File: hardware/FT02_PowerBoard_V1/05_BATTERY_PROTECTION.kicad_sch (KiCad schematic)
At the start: 0 parts

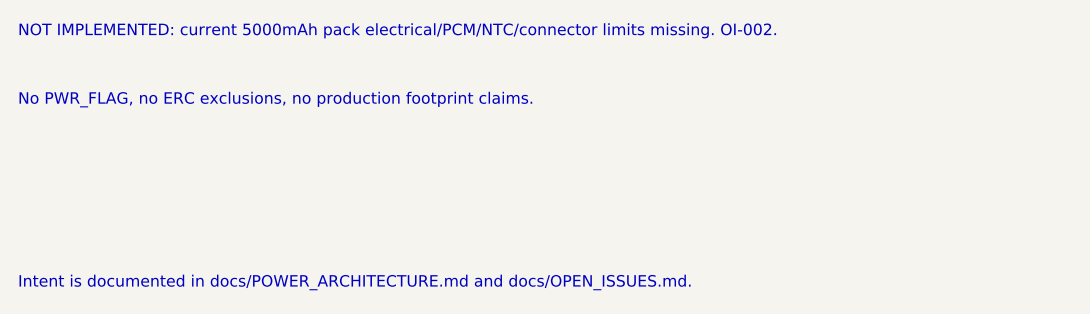
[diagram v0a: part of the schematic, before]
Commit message: 采纳 FT02 电池来源限制并推进 Phase1 电量计参考电路
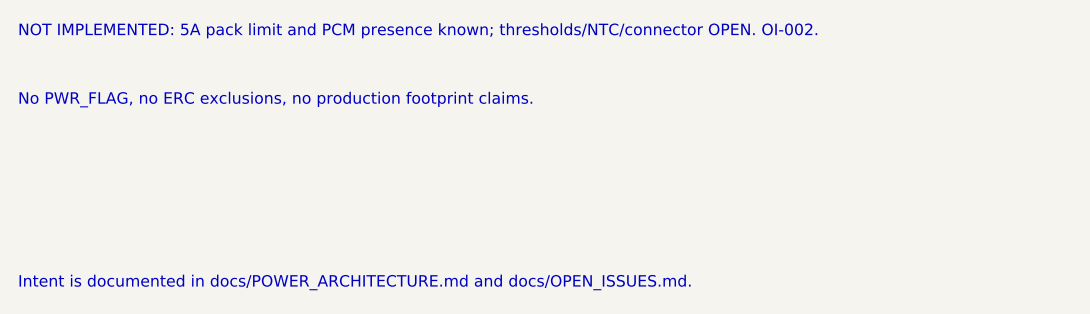
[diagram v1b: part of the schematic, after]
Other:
- note added: "NOT IMPLEMENTED: 5A pack limit and PCM presence known; thresholds/NTC/connector OPEN. OI-002."
- note removed: "NOT IMPLEMENTED: current 5000mAh pack electrical/PCM/NTC/connector limits missing. OI-002."

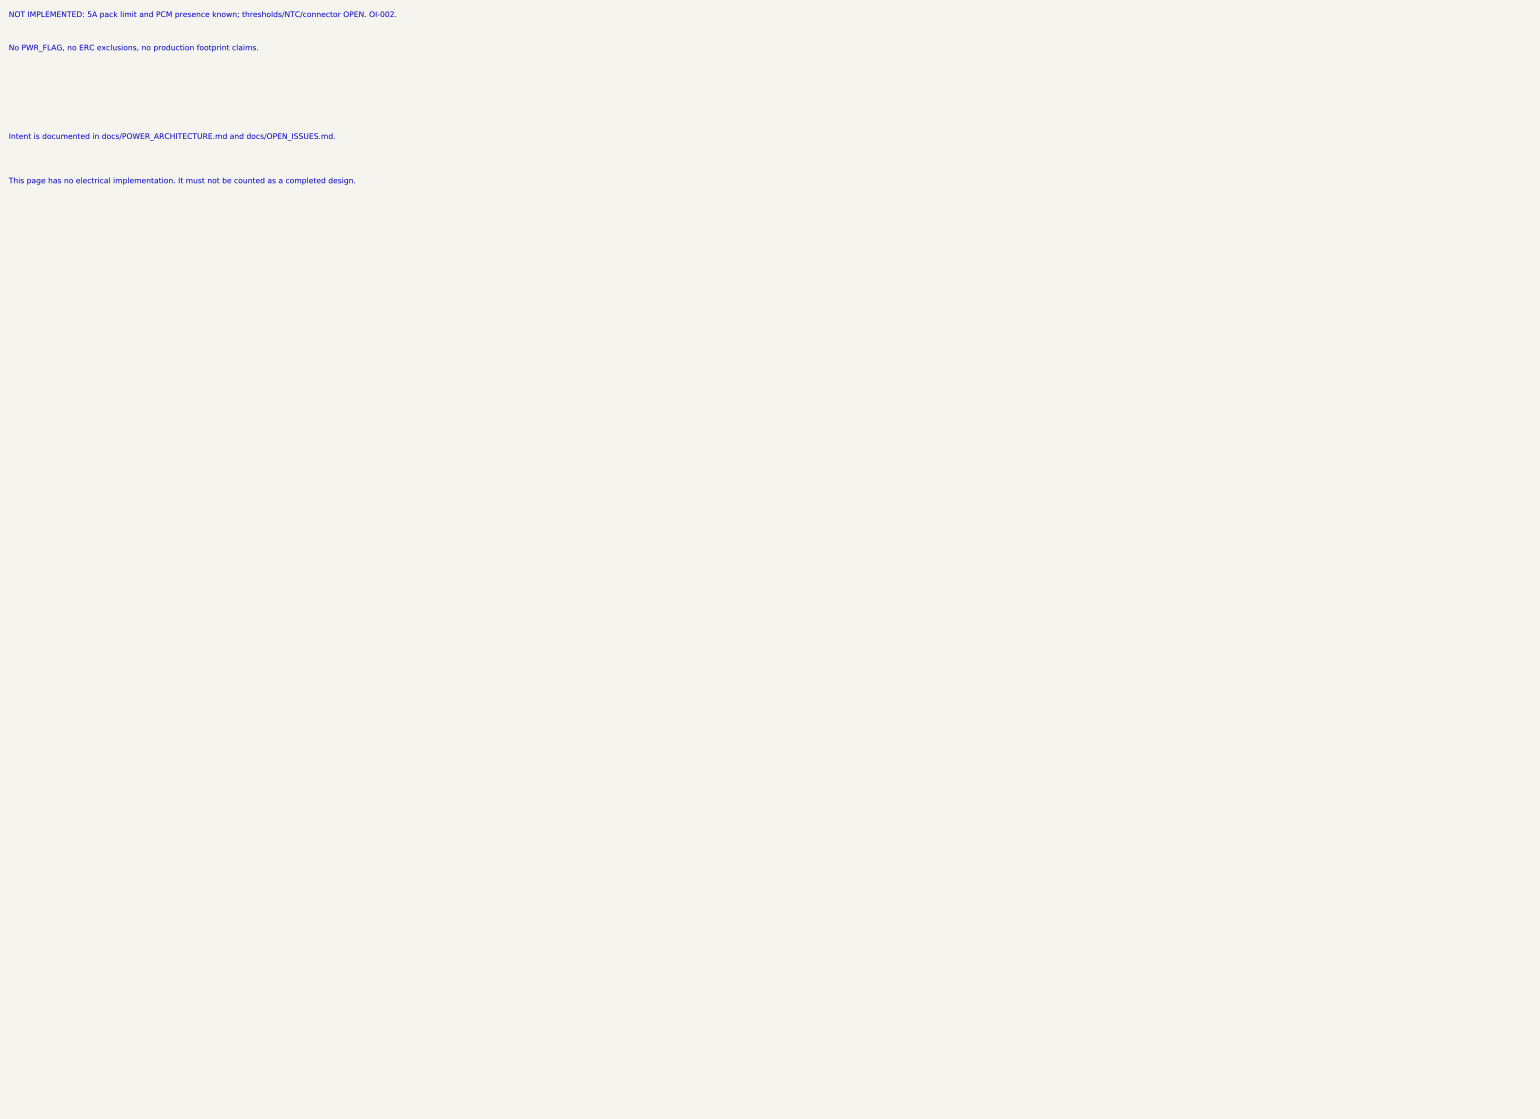
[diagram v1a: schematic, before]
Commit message: Wire FT02 battery guard candidate and export Phase1 review drawings
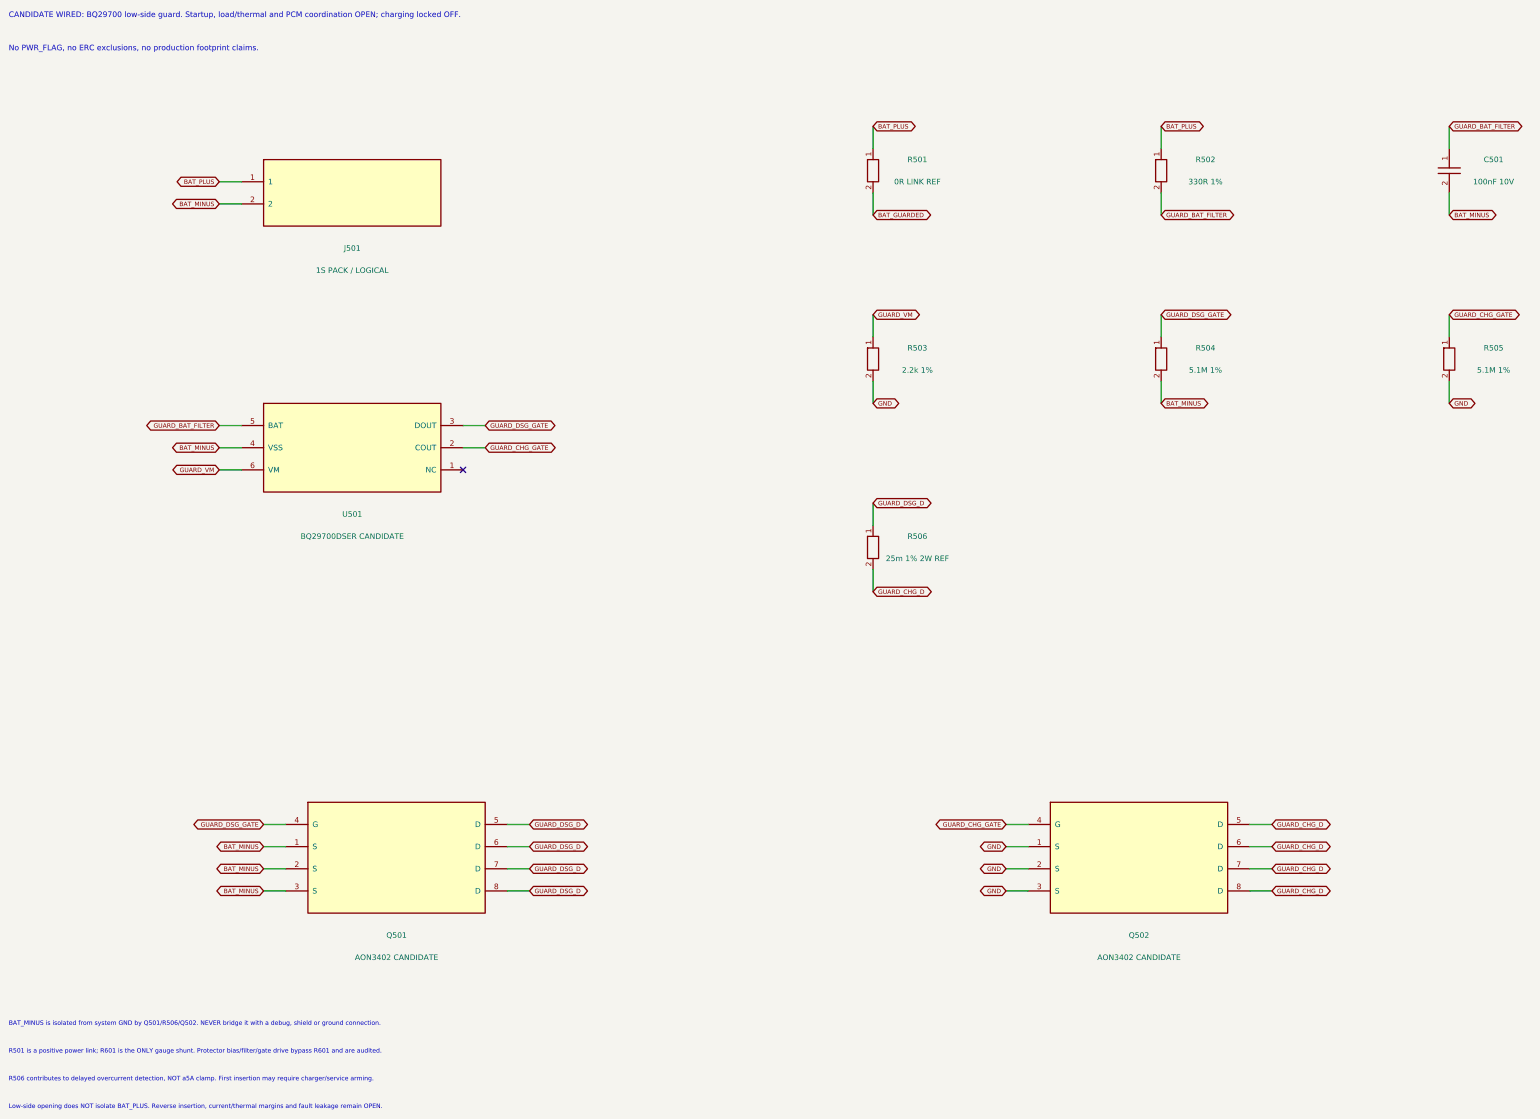
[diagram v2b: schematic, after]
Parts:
- added C501: 100nF 10V, symbol FT02_Reference:C
- added J501: 1S PACK / LOGICAL, symbol FT02_Reference:CONN2
- added Q501, Q502: AON3402 CANDIDATE, symbol FT02_Reference:AON3402
- added R501: 0R LINK REF, symbol FT02_Reference:R
- added R502: 330R 1%, symbol FT02_Reference:R
- added R503: 2.2k 1%, symbol FT02_Reference:R
- added R504, R505: 5.1M 1%, symbol FT02_Reference:R
- added R506: 25m 1% 2W REF, symbol FT02_Reference:R
- added U501: BQ29700DSER CANDIDATE, symbol FT02_Reference:BQ29700
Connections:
- new net BAT_GUARDED: R501.2
- new net BAT_MINUS: C501.2, J501.2, Q501.1 (S), Q501.2 (S), Q501.3 (S), R504.2, U501.4 (VSS)
- new net BAT_PLUS: J501.1, R501.1, R502.1
- new net GND: Q502.1 (S), Q502.2 (S), Q502.3 (S), R503.2, R505.2
- new net GUARD_BAT_FILTER: C501.1, R502.2, U501.5 (BAT)
- new net GUARD_CHG_D: Q502.5 (D), Q502.6 (D), Q502.7 (D), Q502.8 (D), R506.2
- new net GUARD_CHG_GATE: Q502.4 (G), R505.1, U501.2 (COUT)
- new net GUARD_DSG_D: Q501.5 (D), Q501.6 (D), Q501.7 (D), Q501.8 (D), R506.1
- new net GUARD_DSG_GATE: Q501.4 (G), R504.1, U501.3 (DOUT)
- new net GUARD_VM: R503.1, U501.6 (VM)
- no-connect marks 0 -> 1
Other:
- note added: "BAT_MINUS is isolated from system GND by Q501/R506/Q502. NEVER bridge it with a debug, shield or ground connection."
- note added: "CANDIDATE WIRED: BQ29700 low-side guard. Startup, load/thermal and PCM coordination OPEN; charging locked OFF."
- note added: "Low-side opening does NOT isolate BAT_PLUS. Reverse insertion, current/thermal margins and fault leakage remain OPEN."
- note added: "R501 is a positive power link; R601 is the ONLY gauge shunt. Protector bias/filter/gate drive bypass R601 and are audited."
- note added: "R506 contributes to delayed overcurrent detection, NOT a5A clamp. First insertion may require charger/service arming."
- note removed: "Intent is documented in docs/POWER_ARCHITECTURE.md and docs/OPEN_ISSUES.md."
- note removed: "NOT IMPLEMENTED: 5A pack limit and PCM presence known; thresholds/NTC/connector OPEN. OI-002."
- note removed: "This page has no electrical implementation. It must not be counted as a completed design."
